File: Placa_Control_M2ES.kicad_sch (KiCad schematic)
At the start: 0 parts

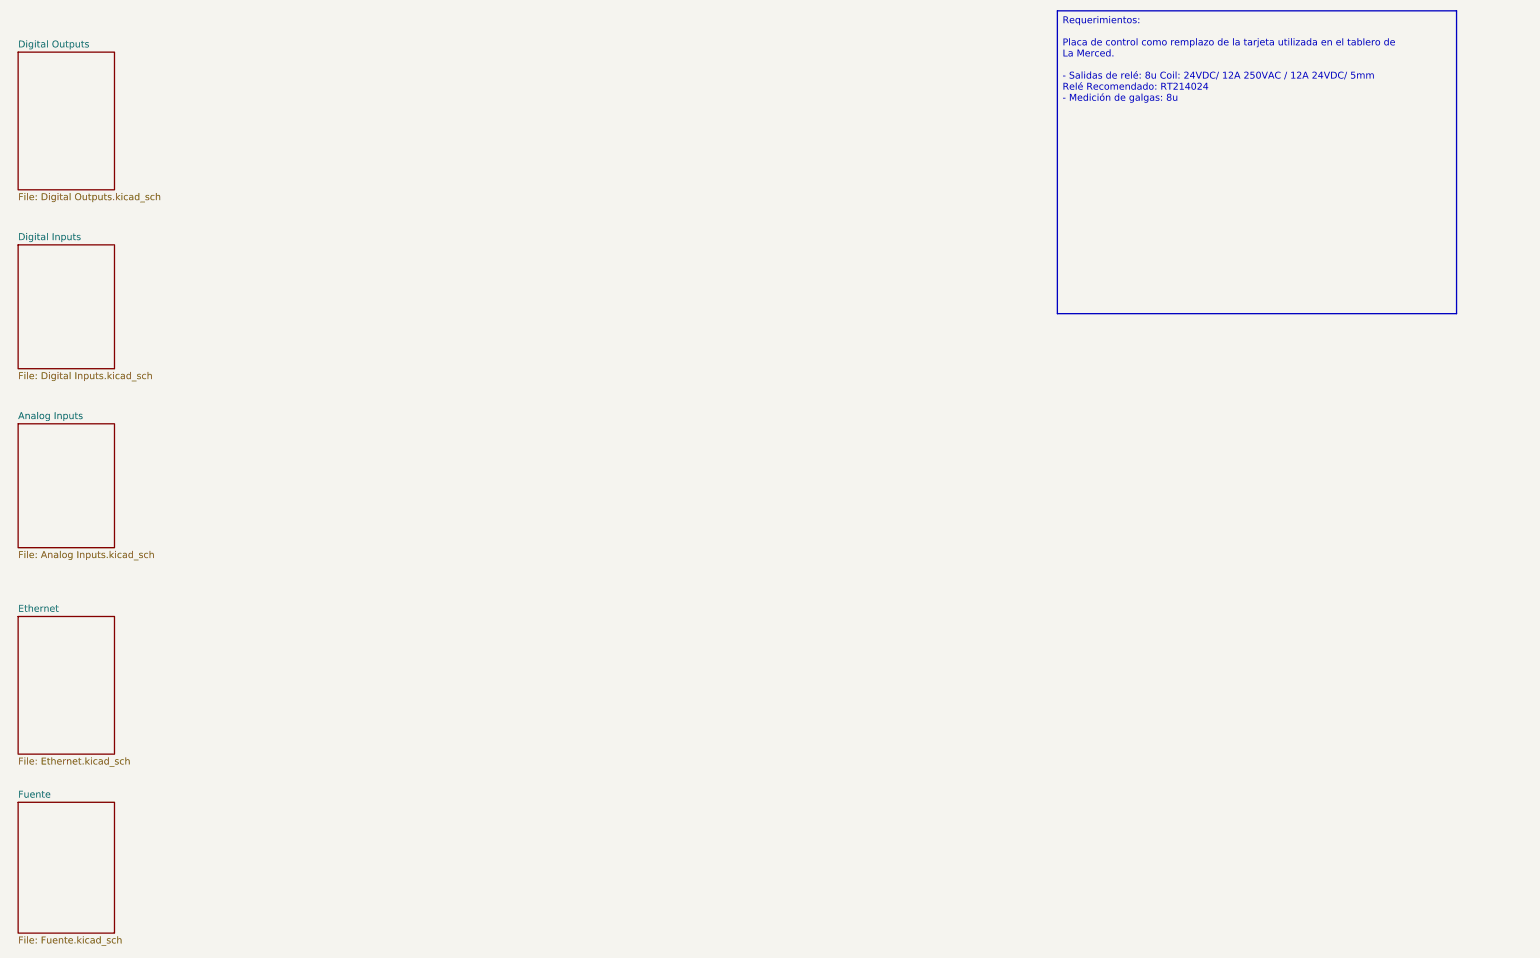
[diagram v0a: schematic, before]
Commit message: Se termina el circuito de entrada análoga, se escoge la bornera. Se termina las salidas de rele, se asumen que se trabajara maximo a 220V y solo para activar contactores. El circuito para el sensor namur se esta realizando
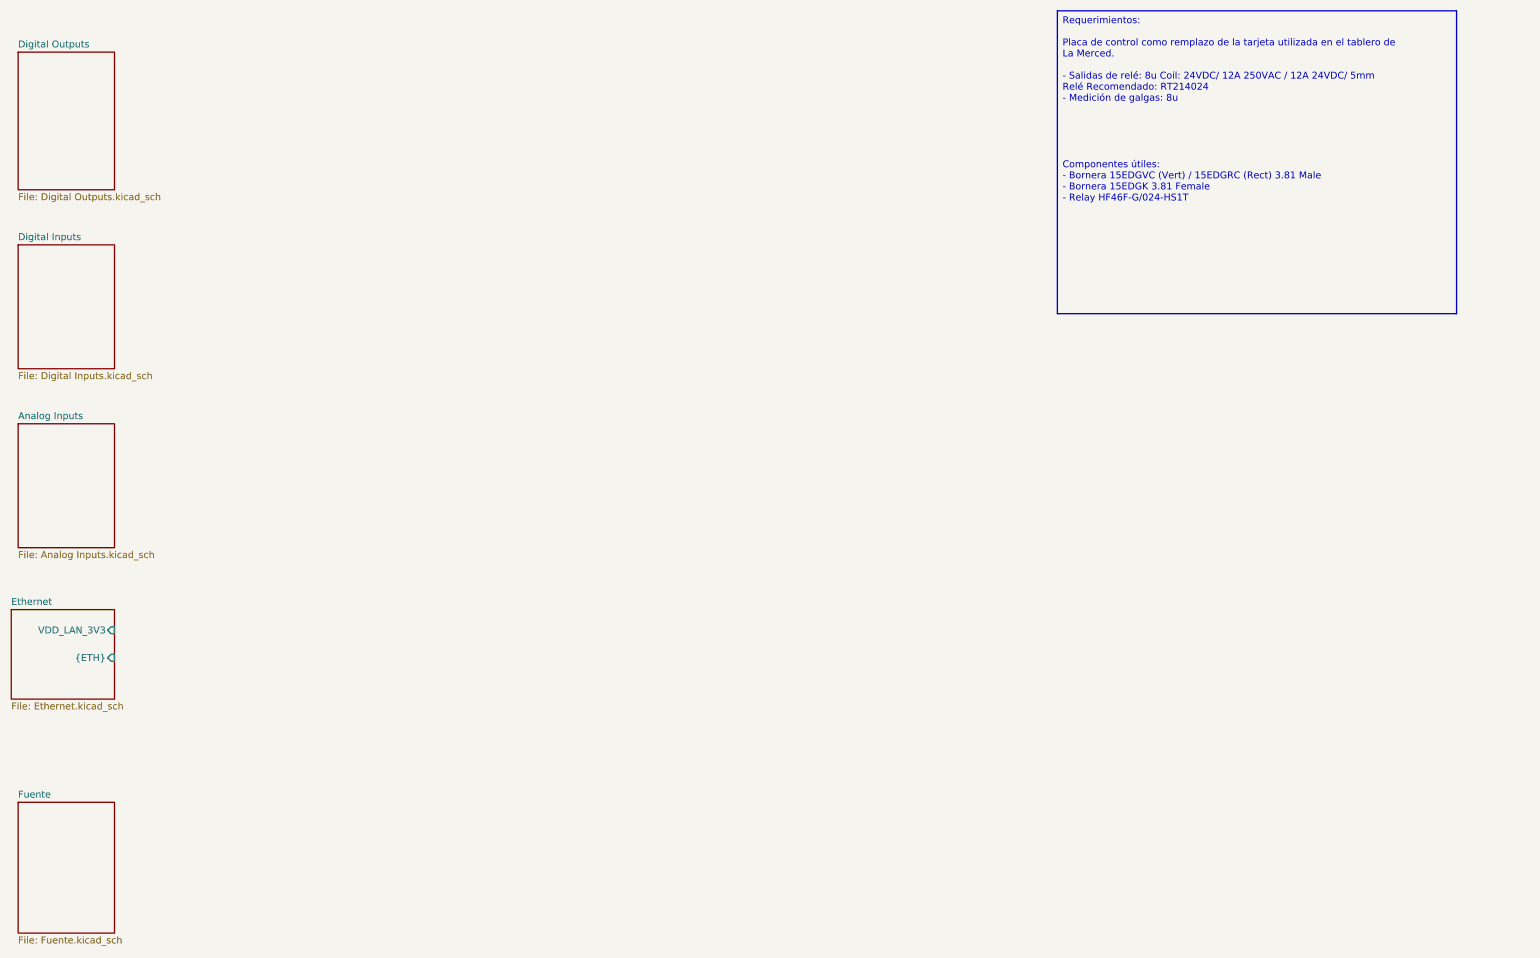
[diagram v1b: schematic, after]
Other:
- sheet Ethernet ports: added VDD_LAN_3V3, {ETH}; removed none
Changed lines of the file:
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@@
 	(generator_version "9.0")
 	(paper "A4")
-	(text_box "Requerimientos:\n\nPlaca de control como remplazo de la tarjeta utilizada en el tablero de La Merced.\n\n- Salidas de relé: 8u Coil: 24VDC/ 12A 250VAC / 12A 24VDC/ 5mm\n  Relé Recomendado: RT214024\n- Medición de galgas: 8u\n"
+	(text_box "Requerimientos:\n\nPlaca de control como remplazo de la tarjeta utilizada en el tablero de La Merced.\n\n- Salidas de relé: 8u Coil: 24VDC/ 12A 250VAC / 12A 24VDC/ 5mm\n  Relé Recomendado: RT214024\n- Medición de galgas: 8u\n\n\n\n\n\nComponentes útiles:\n- Bornera 15EDGVC (Vert) / 15EDGRC (Rect) 3.81 Male\n- Bornera 15EDGK 3.81 Female\n- Relay HF46F-G/024-HS1T"
 		(exclude_from_sim no)
 		(at 208.28 15.24 0)
@@
 	)
 	(sheet
-		(at 16.51 127)
-		(size 17.78 25.4)
+		(at 15.24 125.73)
+		(size 19.05 16.51)
 		(exclude_from_sim no)
 		(in_bom yes)
@@
 		)
 		(property "Sheetname" "Ethernet"
-			(at 16.51 126.2884 0)
+			(at 15.24 125.0184 0)
 			(effects
 				(font
@@
 		)
 		(property "Sheetfile" "Ethernet.kicad_sch"
-			(at 16.51 152.9846 0)
+			(at 15.24 142.8246 0)
 			(effects
 				(font
@@
 			)
 		)
+		(pin "VDD_LAN_3V3" input
+			(at 34.29 129.54 0)
+			(effects
+				(font
+					(size 1.27 1.27)
+				)
+				(justify right)
+			)
+		)
+		(pin "{ETH}" input
+			(at 34.29 134.62 0)
+			(effects
+				(font
+					(size 1.27 1.27)
+				)
+				(justify right)
+			)
+		)
 		(instances
 			(project "Placa_Control_M2ES"
 				(path "/af529cf8-e3d6-4568-89be-bc7010f8b835"
-					(page "5")
+					(page "14")
 				)
 			)

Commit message: Avance
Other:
- added sheet MCU (stm32.kicad_sch)
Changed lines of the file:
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@@
+	)
+	(sheet
+		(at 85.09 71.12)
+		(size 16.51 16.51)
+		(exclude_from_sim no)
+		(in_bom yes)
+		(on_board yes)
+		(dnp no)
+		(fields_autoplaced yes)
+		(stroke
+			(width 0.1524)
+			(type solid)
+		)
+		(fill
+			(color 0 0 0 0.0000)
+		)
+		(property "Sheetname" "MCU"
+			(at 85.09 70.4084 0)
+			(effects
+				(font
+					(size 1.27 1.27)
+				)
+				(justify left bottom)
+			)
+		)
+		(property "Sheetfile" "stm32.kicad_sch"
+			(at 85.09 88.2146 0)
+			(effects
+				(font
+					(size 1.27 1.27)
+				)
+				(justify left top)
+			)
+		)
+		(instances
+			(project "Placa_Control_M2ES"
+				(path "/af529cf8-e3d6-4568-89be-bc7010f8b835"
+					(page "24")
+				)
+			)
+		)
 	)
 	(sheet

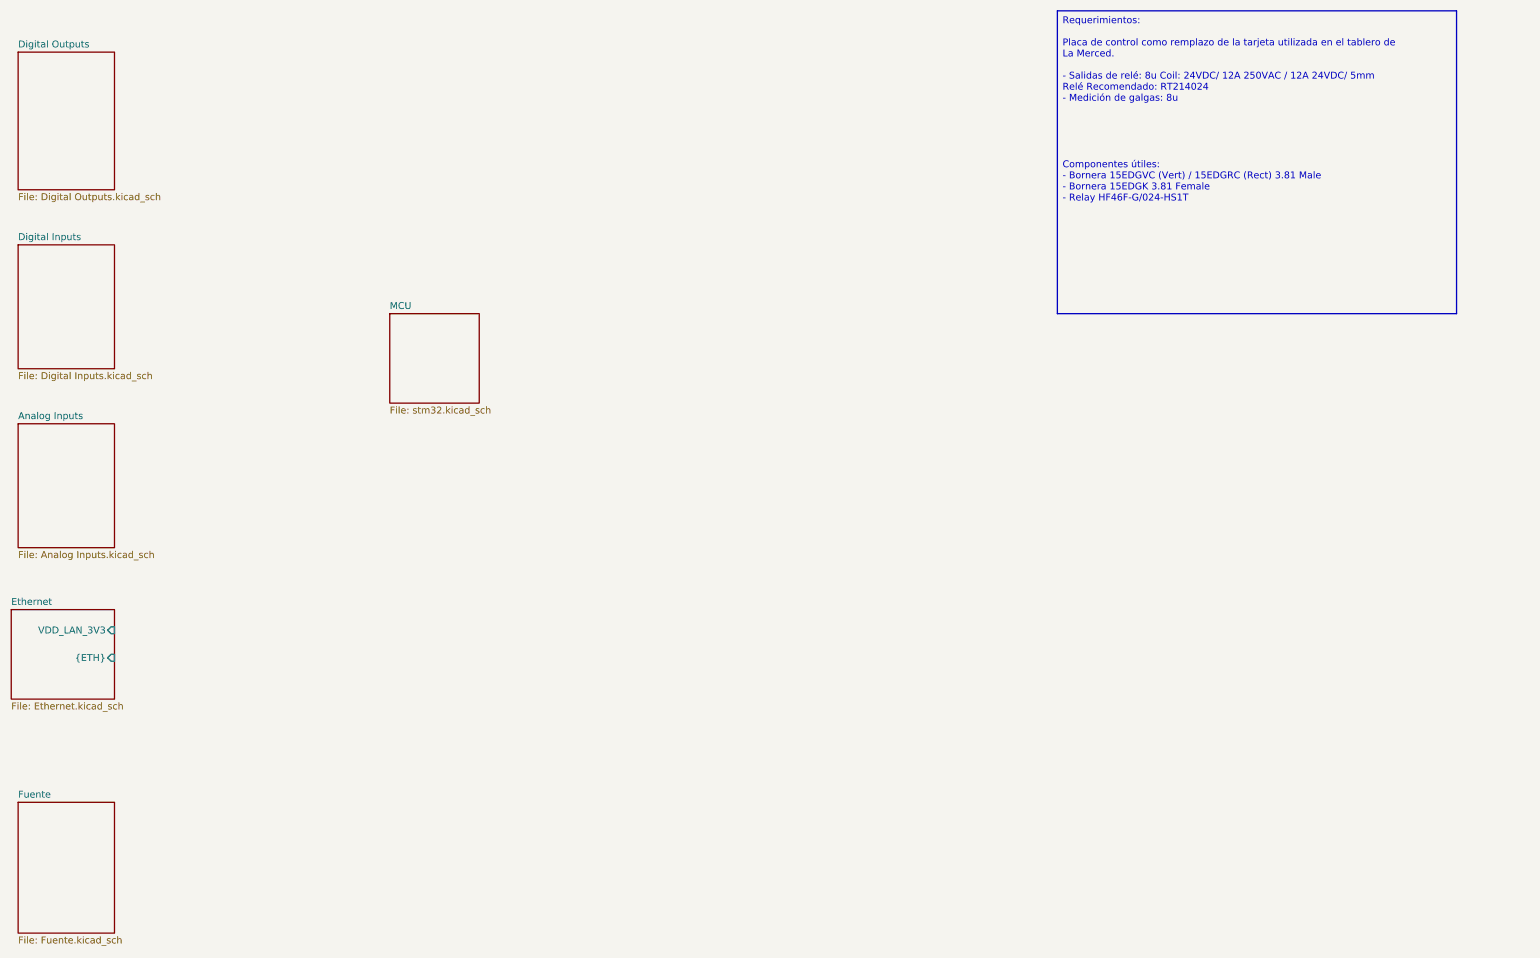
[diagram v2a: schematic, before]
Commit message: avance de pcb, se considera borneras externas para conexión de alimentación
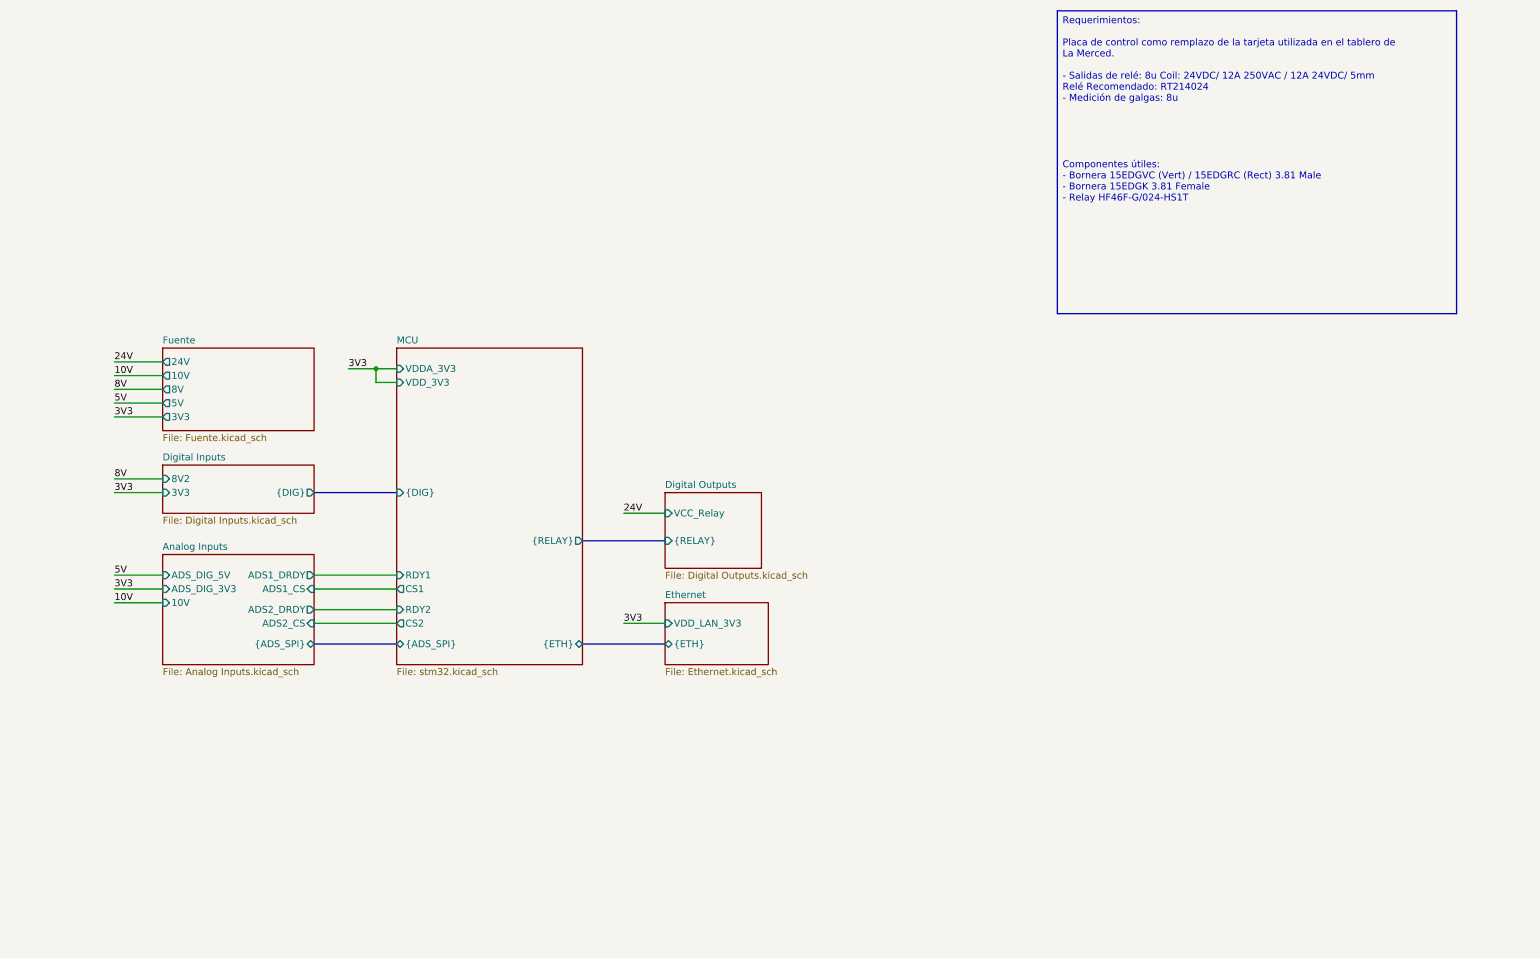
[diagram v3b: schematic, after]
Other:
- sheet Analog Inputs ports: added 10V, ADS1_CS, ADS1_DRDY, ADS2_CS, ADS2_DRDY, ADS_DIG_3V3, ADS_DIG_5V, {ADS_SPI}; removed none
- sheet Digital Inputs ports: added 3V3, 8V2, {DIG}; removed none
- sheet Digital Outputs ports: added VCC_Relay, {RELAY}; removed none
- sheet Fuente ports: added 10V, 24V, 3V3, 5V, 8V; removed none
- sheet MCU ports: added CS1, CS2, RDY1, RDY2, VDDA_3V3, VDD_3V3, {ADS_SPI}, {DIG}, {ETH}, {RELAY}; removed none

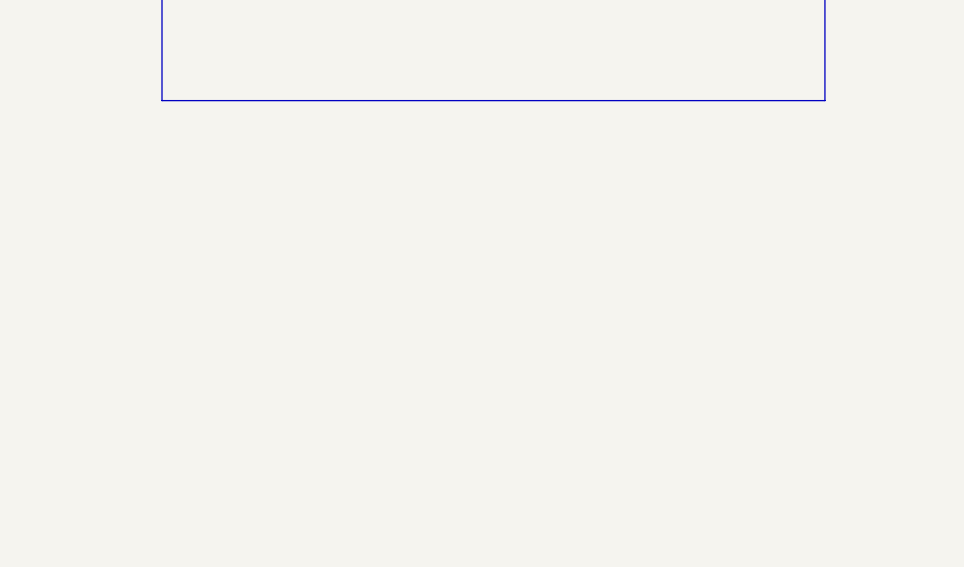
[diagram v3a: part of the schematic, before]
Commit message: Se crea nueva version debido a que el anterior diseño estaba para un uC stm32h7. Este nuevo diseño corresponde al stm32f407v utilizado en el esterilizador y otros proyectos conocidos en la empresa.
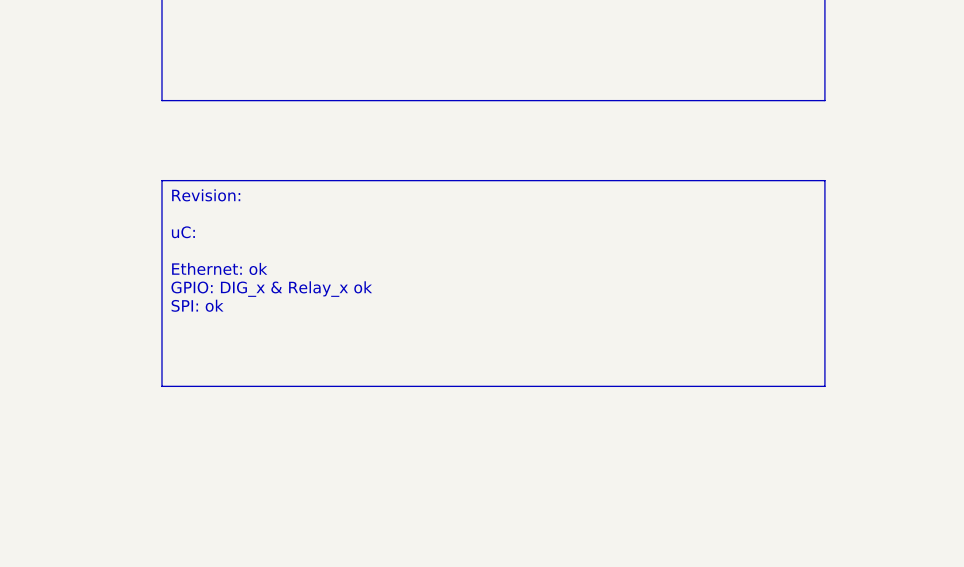
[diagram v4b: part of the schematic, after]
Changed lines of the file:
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@@
+		)
+	)
+	(text_box "Revision:\n\nuC:\n\nEthernet: ok\nGPIO: DIG_x & Relay_x ok\nSPI: ok\n"
+		(exclude_from_sim no)
+		(at 208.28 80.01 0)
+		(size 73.66 22.86)
+		(margins 0.9525 0.9525 0.9525 0.9525)
+		(stroke
+			(width 0)
+			(type solid)
+		)
+		(fill
+			(type none)
+		)
+		(effects
+			(font
+				(size 1.27 1.27)
+			)
+			(justify left top)
 		)
 	)
